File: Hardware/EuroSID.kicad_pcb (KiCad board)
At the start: 2 copper layers, 213.3 x 106.6 mm, 228 parts, among them J1 GATE_2, J10 IN_2, J11 IN_3, J12 PWM_CV, J13 EXT_CON, J14 Conn_01x04_Female, J15 Eurorack Connector, J16 Conn_01x06_Male, J17 Conn_ARM_JTAG_SWD_10, J18 Power_Connector_IO, J19 Power_Connector, J2 GATE_3, J20 Digital_Connector_IO, J21 CV_Connector_IO, J22 Pot_Connector_IO, J23 Attenuverter_Connector_IO, J24 Digital_Connector, J25 CV_Connector, J26 Pot_Connector, J27 Attenuverter_Connector, J28 SID_Audio_Connector_IO, J29 SID_Audio_Connector, J3 GATE_1, J4 OUT2_CON, J5 CUTOFF_CV, J6 SHAPE_CV, J7 SET_CV, J8 OUT1_CON, J9 IN_1, Q1 MMBT3904, Q2 MMBT3904, Q3 MMBT3904, SW1 Frequency Adjust, SW10 SET_SW, SW11 FILTER_SW, SW12 FILTEREXT_SW, SW13 SHAPE_SW, SW2 MOD_SW, SW3 FILTER1_SW, SW4 PROG, SW5 VOICE_SW, SW6 FILTER2_SW, SW7 RST, SW8 MODE_SW, SW9 FILTER3_SW, U1 TLC5947DAP, U10 LM1117-3.3, U11 LM1117-5.0, U12 L7809, U13 STM32F303RBTx, U2 OPA1678, U3 MCP6004, U4 MCP6004, U6 74HC595, U7 74HC595, U8 SID, U9 LM1117-3.3, X1 ECS-8FMX-010-TR

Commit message: Added 3D model of fader
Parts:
- moved R11 127.1 mm to (165.2, 122.9), turned to 180 degrees
- moved R9 120.0 mm to (172.5, 122.9), turned to 180 degrees
- moved R12 109.3 mm to (180.1, 122.9), turned to 180 degrees
- moved Q1 109.1 mm to (161.3, 123.1)
- moved R8 107.3 mm to (157.5, 122.9), turned to 180 degrees
- moved Q2 97.6 mm to (176.3, 123.1)
- moved Q3 86.3 mm to (191.0, 123.0)
- moved D24 82.9 mm to (220.2, 134.8)
- moved R10 77.6 mm to (187.3, 122.9), turned to 180 degrees
- moved R13 69.8 mm to (194.9, 122.9), turned to 180 degrees
- moved H1 4.19 mm to (121.2, 89.7)
- moved H5 4.19 mm to (233.0, 89.7)
- moved J12 1.61 mm to (206.1, 136.7)
- turned J5 to 270 degrees
- turned RV1 to 90 degrees
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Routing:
- net 3.3_IO: track 0.00 -> 464.3 mm
- net 3.3A_IO: track 0.00 -> 277.4 mm
- net GND: track 88.9 -> 319.2 mm, vias 4 -> 104
- net FILTER3_SW: track 0.00 -> 227.0 mm, vias 0 -> 5
- net FILTER2_SW: track 0.00 -> 222.5 mm, vias 0 -> 3
- net FILTEREXT_SW: track 0.00 -> 221.5 mm, vias 0 -> 3
- net FILTER1_SW: track 0.00 -> 207.5 mm, vias 0 -> 3
- net FREQ_A: track 0.00 -> 190.7 mm, vias 0 -> 8
- net VOICE_SW: track 0.00 -> 161.1 mm, vias 0 -> 2
- net SET_SW: track 0.00 -> 160.1 mm, vias 0 -> 7
- net SHAPE_SW: track 0.00 -> 153.2 mm, vias 0 -> 5
- net FILTER_SW: track 0.00 -> 149.8 mm, vias 0 -> 5
- net PWM_CV: track 0.00 -> 137.1 mm, vias 0 -> 1
- net SET_CV: track 0.00 -> 136.6 mm, vias 0 -> 1
- net MODE_SW: track 0.00 -> 124.2 mm, vias 0 -> 7
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
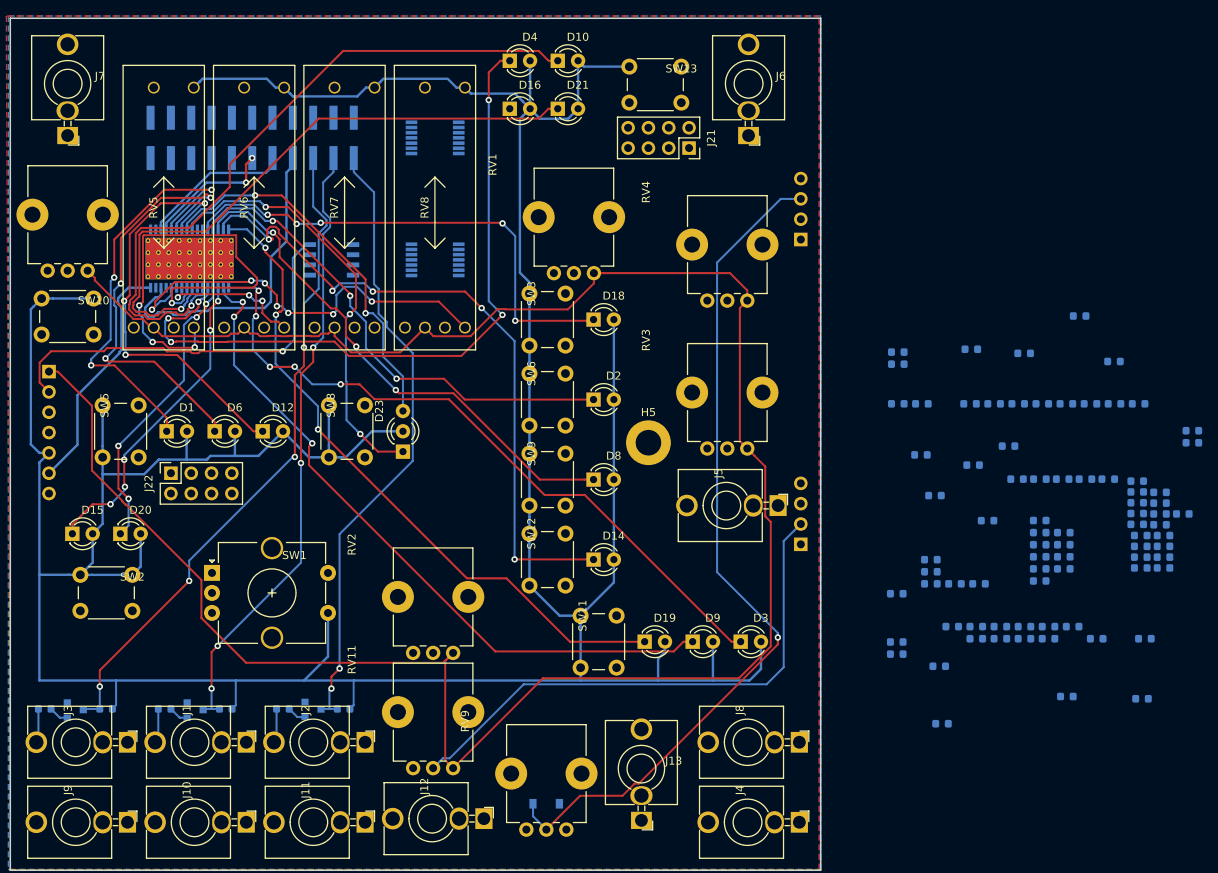
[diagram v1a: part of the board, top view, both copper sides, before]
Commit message: Routed 1st opamp, audio opamp
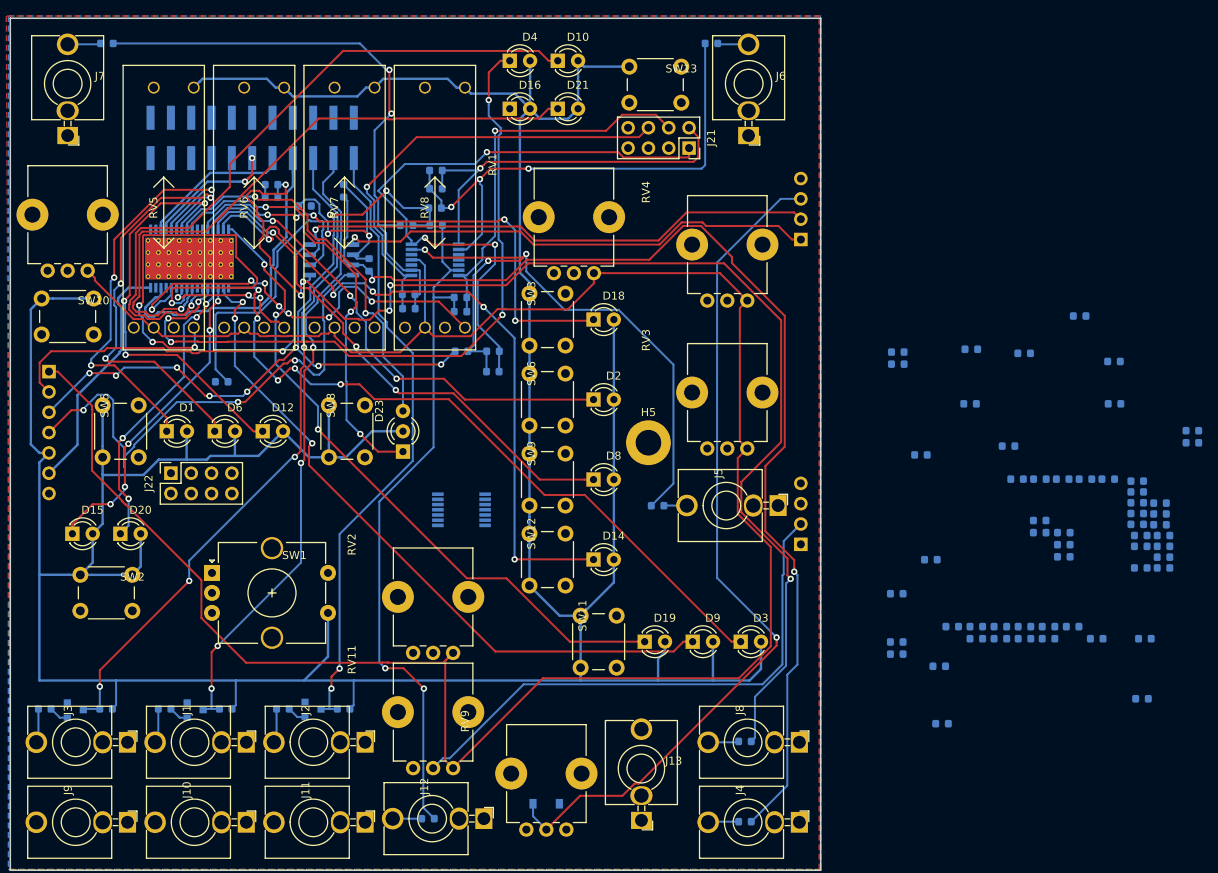
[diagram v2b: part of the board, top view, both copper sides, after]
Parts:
- moved R35 136.5 mm to (165.3, 39.7)
- moved C27 117.0 mm to (185.9, 58.9), turned to 180 degrees
- moved C14 109.7 mm to (194.9, 58.2), turned to 90 degrees
- moved R29 108.1 mm to (185.9, 57.4)
- moved R48 102.9 mm to (205.4, 136.7)
- moved C28 102.8 mm to (206.4, 55.6), turned to 180 degrees
- moved R28 102.6 mm to (179.6, 82.0), turned to 180 degrees
- moved R25 89.6 mm to (190.0, 60.1)
- moved R36 88.4 mm to (206.4, 57.9)
- moved R38 86.3 mm to (203.0, 71.1), turned to 180 degrees
- moved R26 83.0 mm to (198.0, 67.4), turned to 270 degrees
- moved R30 82.6 mm to (206.3, 60.3)
- moved C29 82.5 mm to (213.5, 80.8), turned to 180 degrees
- moved R34 81.9 mm to (202.7, 62.5), turned to 180 degrees
- moved R47 81.3 mm to (206.4, 62.5)
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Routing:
- net Net-(C27-Pad1): track 0.00 -> 156.7 mm, vias 0 -> 6
- net Net-(C14-Pad1): track 0.00 -> 141.3 mm, vias 0 -> 2
- net -10V_REF_IO: track 0.00 -> 96.6 mm, vias 0 -> 10
- net Net-(C34-Pad2): track 0.00 -> 87.9 mm, vias 0 -> 2
- net Net-(C29-Pad2): track 0.00 -> 81.0 mm, vias 0 -> 3
- net CUTOFF_CV_IO: track 0.00 -> 79.7 mm, vias 0 -> 3
- net Net-(C30-Pad2): track 0.00 -> 73.5 mm, vias 0 -> 2
- net SID1_OUT_IO: track 0.00 -> 67.4 mm, vias 0 -> 1
- net Net-(C28-Pad2): track 0.00 -> 66.4 mm, vias 0 -> 3
- net 12V_IO: track 0.00 -> 65.8 mm, vias 0 -> 3
- net SID2_OUT_IO: track 0.00 -> 60.2 mm, vias 0 -> 1
- net SET_CV_IO: track 0.00 -> 57.1 mm, vias 0 -> 1
- net SHAPE_CV_IO: track 0.00 -> 49.8 mm, vias 0 -> 1
- net PWM_CV_IO: track 0.00 -> 49.0 mm, vias 0 -> 1
- net Net-(C27-Pad2): track 0.00 -> 38.6 mm
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
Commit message: Finishing up PCB
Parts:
- moved R1 123.1 mm to (160.6, 74.0)
- moved C2 120.4 mm to (174.6, 113.8), turned to 180 degrees
- moved R46 113.7 mm to (190.5, 137.5)
- moved R44 111.4 mm to (175.8, 133.3)
- moved R5 102.8 mm to (171.2, 108.7)
- moved R3 99.4 mm to (174.6, 111.2), turned to 180 degrees
- moved R2 89.4 mm to (182.2, 102.4)
- moved R43 88.4 mm to (196.5, 102.2)
- moved C1 87.9 mm to (182.2, 106.2), turned to 180 degrees
- moved C31 85.6 mm to (204.1, 95.6), turned to 180 degrees
- moved R41 83.9 mm to (201.2, 98.0)
- moved R42 78.4 mm to (206.6, 105.3)
- moved R15 72.6 mm to (226.4, 77.5)
- moved R49 69.2 mm to (205.8, 93.3)
- moved C32 67.2 mm to (210.6, 92.7)
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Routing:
- net -10V_REF_IO: track 96.6 -> 201.2 mm, vias 10 -> 12
- net Net-(C32-Pad2): track 0.00 -> 98.4 mm, vias 0 -> 4
- net FILTEREXT_SW_IO: track 0.00 -> 92.9 mm, vias 0 -> 2
- net FILTER3_SW_IO: track 0.00 -> 87.7 mm, vias 0 -> 2
- net IN3_CV_IO: track 0.00 -> 86.9 mm, vias 0 -> 4
- net Net-(J10-PadTN): track 0.00 -> 80.4 mm, vias 0 -> 1
- net FILTER1_SW_IO: track 0.00 -> 77.2 mm, vias 0 -> 3
- net IN1_CV_IO: track 0.00 -> 75.0 mm, vias 0 -> 1
- net Net-(C33-Pad2): track 0.00 -> 70.6 mm, vias 0 -> 2
- net Net-(C31-Pad2): track 0.00 -> 33.6 mm, vias 0 -> 2
- net Net-(J10-PadT): track 0.00 -> 29.9 mm
- net 3.3A_IO: track 287.4 -> 313.7 mm
- net Net-(R1-Pad2): track 0.00 -> 17.6 mm, vias 0 -> 2
- net Net-(R40-Pad1): track 0.00 -> 13.6 mm
- net IN2_CV_IO: track 0.00 -> 12.2 mm, vias 0 -> 2
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
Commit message: Tried making board 100x100
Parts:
- moved R22 124.4 mm to (160.9, 78.4)
- moved R17 122.8 mm to (161.6, 94.0), turned to 270 degrees
- moved R14 116.6 mm to (169.4, 113.8)
- moved R7 104.8 mm to (190.9, 101.8), turned to 90 degrees
- moved R20 91.2 mm to (193.8, 94.9), turned to 180 degrees
- moved C4 90.7 mm to (189.2, 108.5), turned to 270 degrees
- moved R6 87.7 mm to (193.0, 101.9), turned to 90 degrees
- moved R56 58.6 mm to (236.4, 39.2), turned to 90 degrees
- moved J27 0.17 mm to (140.1, 102.3)
- moved J29 0.09 mm to (140.2, 64.3)
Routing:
- net MODE_SW_IO: track 0.00 -> 139.5 mm, vias 0 -> 5
- net FILTER2_SW_IO: track 9.39 -> 119.4 mm, vias 0 -> 5
- net VOICE_SW_IO: track 0.00 -> 106.8 mm, vias 0 -> 5
- net SHAPE_SW_IO: track 0.00 -> 92.5 mm, vias 0 -> 2
- net MOD_SW_IO: track 0.00 -> 81.8 mm, vias 0 -> 2
- net FREQ_SW_IO: track 0.00 -> 79.7 mm, vias 0 -> 4
- net PWM_ATTEN: track 66.4 -> 0.00 mm
- net SET_SW_IO: track 0.00 -> 47.1 mm, vias 0 -> 1
- net Net-(D10-Pad1): track 87.0 -> 123.1 mm
- net Net-(C27-Pad2): track 38.6 -> 54.8 mm, vias 0 -> 2
- net 3.3_IO: track 471.1 -> 482.1 mm
- net Net-(R6-Pad1): track 0.00 -> 5.34 mm
- net SID1_EXT: track 33.0 -> 30.1 mm, vias 0 -> 3
- net Net-(C27-Pad1): track 156.7 -> 154.1 mm
- net GATE_3_IO: track 78.3 -> 80.5 mm
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- removed copper zone on F.Cu, net (none)
- removed copper zone on B.Cu, net GND
- removed copper zone on F.Cu, net GND
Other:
- board size 213.3 x 106.6 mm -> 211.9 x 106.6 mm

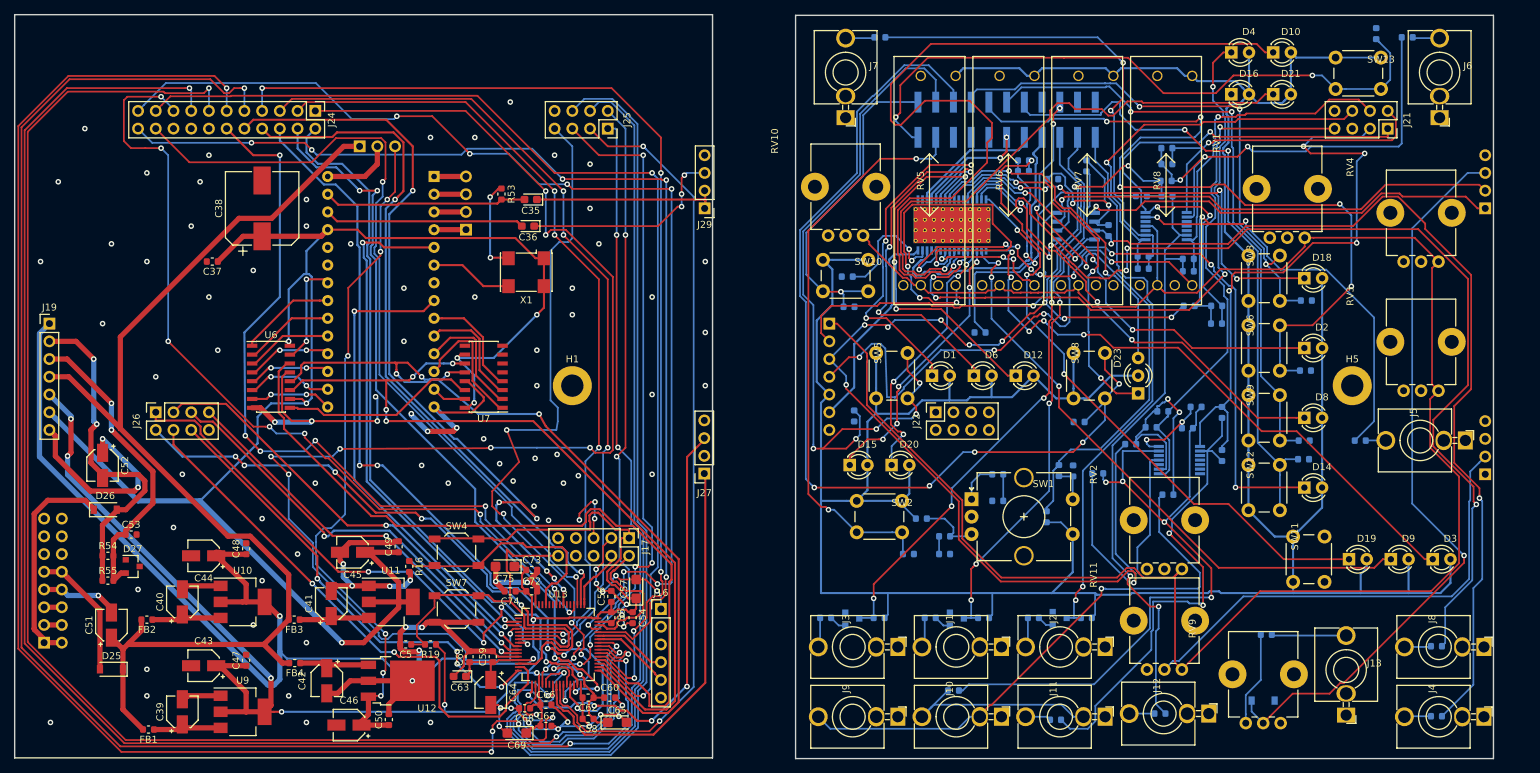
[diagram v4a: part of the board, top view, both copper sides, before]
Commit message: Updated PCBnew to reflect new panel layout
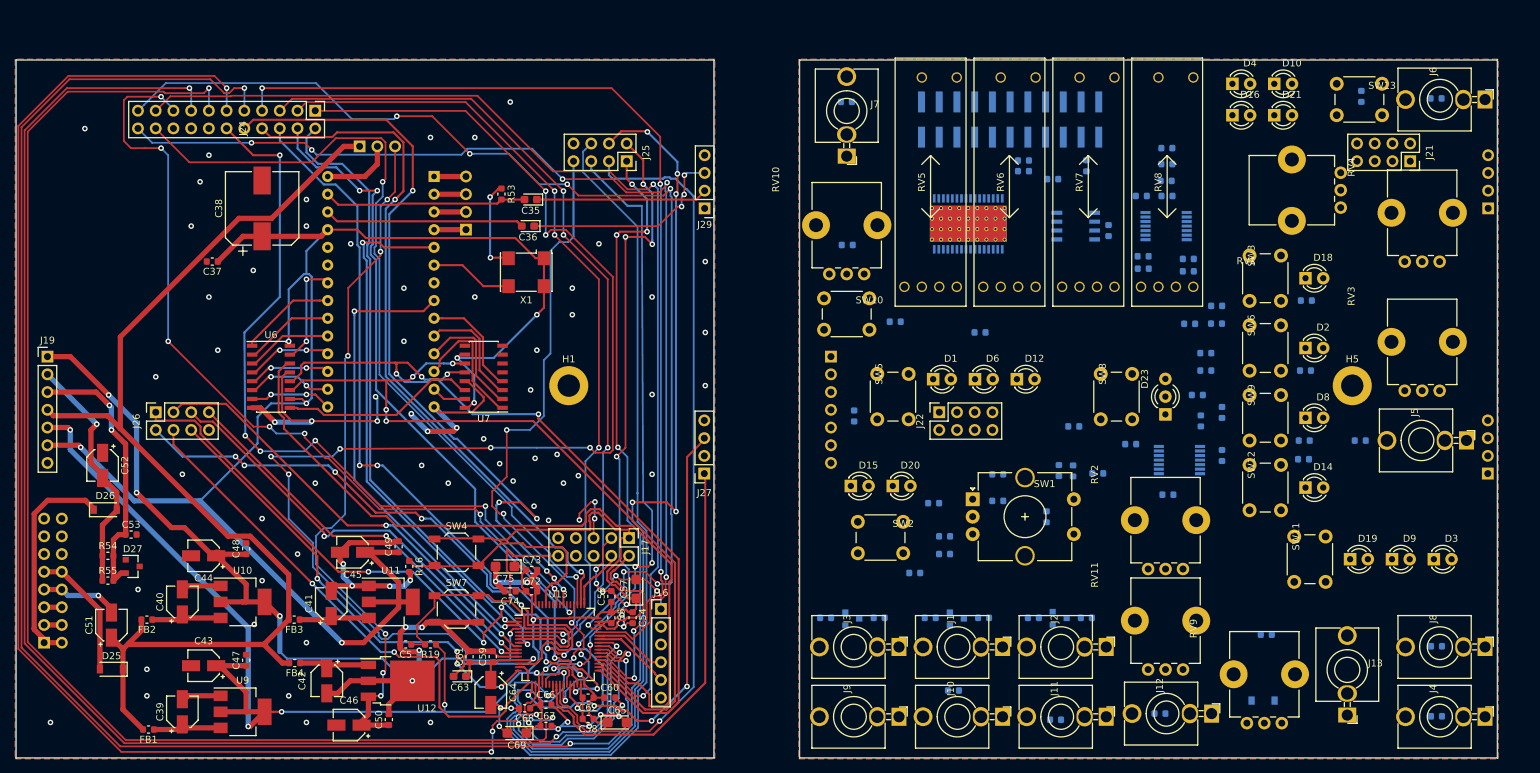
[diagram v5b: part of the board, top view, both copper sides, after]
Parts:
- moved J24 12.8 mm to (71.7, 51.5)
- moved R50 11.1 mm to (212.0, 85.0)
- moved R35 10.4 mm to (160.5, 49.0)
- moved R31 9.68 mm to (245.0, 48.5)
- moved R56 9.25 mm to (234.3, 48.2)
- moved C31 7.19 mm to (211.3, 94.7), turned to 270 degrees
- moved R22 6.96 mm to (167.5, 80.5)
- moved J21 5.67 mm to (241.3, 57.5)
- moved J7 5.51 mm to (160.5, 50.4)
- moved RV10 5.51 mm to (160.5, 66.2)
- moved SW10 5.51 mm to (160.5, 79.4)
- moved R49 5.48 mm to (210.8, 91.0)
- moved J25 5.40 mm to (129.0, 57.5)
- moved C32 5.39 mm to (212.0, 87.5)
- moved D23 4.92 mm to (206.2, 91.2)
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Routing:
- net 3.3_IO: track 482.1 -> 0.00 mm
- net 3.3A_IO: track 313.7 -> 0.00 mm
- net -10V_REF_IO: track 200.3 -> 0.00 mm, vias 12 -> 0
- net Net-(C27-Pad1): track 154.1 -> 0.00 mm, vias 6 -> 0
- net Net-(C14-Pad1): track 141.3 -> 0.00 mm, vias 2 -> 0
- net MODE_SW_IO: track 139.5 -> 0.00 mm, vias 5 -> 0
- net Net-(D10-Pad1): track 123.1 -> 0.00 mm, vias 1 -> 0
- net FILTER2_SW_IO: track 119.4 -> 0.00 mm, vias 5 -> 0
- net SID1_EXT_IO: track 107.0 -> 0.00 mm, vias 1 -> 0
- net VOICE_SW_IO: track 106.8 -> 0.00 mm, vias 5 -> 0
- net Net-(C32-Pad2): track 98.4 -> 0.00 mm, vias 4 -> 0
- net FILTEREXT_SW_IO: track 92.9 -> 0.00 mm, vias 2 -> 0
- net SHAPE_SW_IO: track 92.5 -> 0.00 mm, vias 2 -> 0
- net Net-(D4-Pad1): track 90.7 -> 0.00 mm, vias 5 -> 0
- net Net-(D3-Pad1): track 89.6 -> 0.00 mm, vias 5 -> 0
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- added copper zone on B.Cu, net GND
- added copper zone on F.Cu, net GND
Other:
- board size 211.9 x 106.6 mm -> 212.3 x 100 mm

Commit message: More routing on IO board
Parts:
- moved R29 15.6 mm to (191.5, 72.0)
- moved C27 15.6 mm to (194.7, 71.7)
- moved C14 13.8 mm to (198.1, 71.6)
- moved R25 8.61 mm to (198.4, 62.1)
- moved U1 0.97 mm to (177.9, 65.5)
- turned R31 to 0 degrees
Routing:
- net 3.3_IO: track 0.00 -> 454.9 mm
- net 3.3A_IO: track 0.00 -> 341.2 mm, vias 0 -> 2
- net Net-(D9-Pad1): track 0.00 -> 122.8 mm, vias 0 -> 4
- net FREQ_A_IO: track 0.00 -> 104.8 mm, vias 0 -> 6
- net FILTEREXT_SW_IO: track 0.00 -> 101.1 mm, vias 0 -> 2
- net Net-(D3-Pad1): track 0.00 -> 99.6 mm, vias 0 -> 2
- net Net-(D19-Pad1): track 0.00 -> 87.8 mm, vias 0 -> 4
- net FILTER3_SW_IO: track 0.00 -> 83.4 mm, vias 0 -> 3
- net Net-(D23-Pad3): track 0.00 -> 82.9 mm, vias 0 -> 2
- net Net-(D1-Pad1): track 0.00 -> 82.5 mm, vias 0 -> 5
- net FILTER2_SW_IO: track 0.00 -> 79.2 mm, vias 0 -> 3
- net Net-(D14-Pad1): track 0.00 -> 74.4 mm, vias 0 -> 3
- net FILTER1_SW_IO: track 0.00 -> 73.2 mm, vias 0 -> 2
- net -10V_REF_IO: track 0.00 -> 71.6 mm, vias 0 -> 6
- net Net-(D23-Pad1): track 0.00 -> 69.6 mm, vias 0 -> 3
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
